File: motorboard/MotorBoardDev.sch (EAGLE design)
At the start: 65 parts, among them J1 Under Glow, J2 B2PS-VH(LF)(SN), J3 B2PS-VH(LF)(SN), J4 B2PS-VH(LF)(SN), Q1 SSM3J338R, Q2 SSM3J338R, Q3 SSM3J338R, Q4 STT4P3LLH6, U1 TXB0104DR, U2 9DoF IMU, U3 TXB0106PWR, U4 TLV70233DBVR, X1 C-GRID-05-15-91, X2 C-GRID-05-15-91, X3 MINI-USB_SHIELD5P4-32005-400, X4 C-GRID-02-70553, X5 SI-50170, X7 2510-, X8 2510-

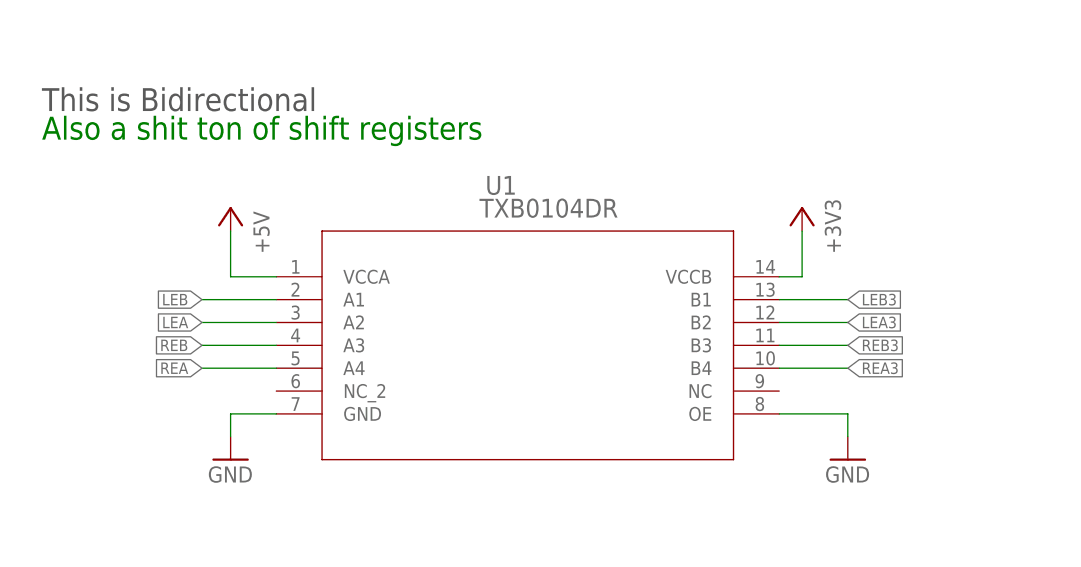
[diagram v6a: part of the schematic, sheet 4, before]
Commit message: Differential and Silkscreen fixed
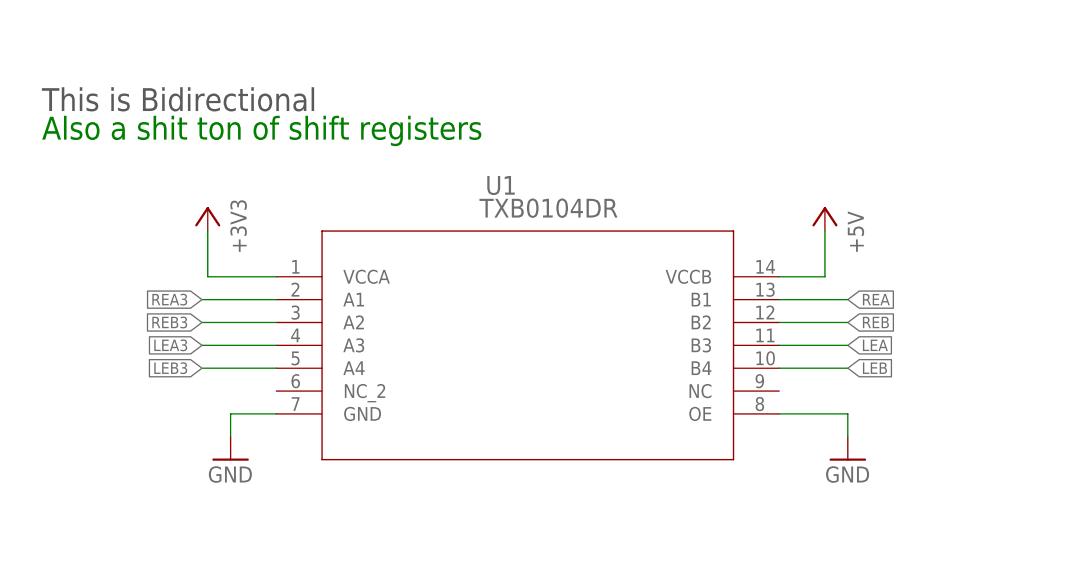
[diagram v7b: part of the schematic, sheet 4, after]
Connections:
- net N$1 renamed SAFETY_HRD
- net N$10 renamed FRONT_HDR
- net N$12 renamed 12V_LED_R
- net N$17 renamed MBED_R_LED1
- net N$18 renamed MBED_R_LED2
- net N$19 renamed GREEN_R
- net N$2 renamed REGOUT_C
- net N$26 renamed RED_R
- net N$29 renamed R_OK3A
- net N$3 renamed INDI_LED_R
- net N$30 renamed R_OK4A
- net N$31 renamed R_OK4B
- net N$32 renamed R_OK3B
- net N$4 renamed BLUE_R
- net N$5 renamed 5V_LED_R
- net N$6 renamed 3V3_LED_R
- net N$7 renamed SAFETY_R
- net N$8 renamed FRONT_R
- net N$9 renamed 24V_LED_R
- net +3V3: now also U1.VCCA; no longer U1.VCCB
- net +5V: now also U1.VCCB; no longer U1.VCCA
- net LEA: now also U1.B3; no longer U1.A2
- net LEA3: now also U1.A3; no longer U1.B2
- net LEB: now also U1.B4; no longer U1.A1
- net LEB3: now also U1.A4; no longer U1.B1
- net REA: now also U1.B1; no longer U1.A4
- net REA3: now also U1.A1; no longer U1.B4
- net REB: now also U1.B2; no longer U1.A3
- net REB3: now also U1.A2; no longer U1.B3
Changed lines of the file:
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@@
 </segment>
 </net>
-<net name="N$17" class="0">
+<net name="MBED_R_LED1" class="0">
 <segment>
 <pinref part="A1" gate="G$1" pin="P$22"/>
@@
 </segment>
 </net>
-<net name="N$18" class="0">
+<net name="MBED_R_LED2" class="0">
 <segment>
 <pinref part="A1" gate="G$1" pin="P$21"/>
@@
 </segment>
 </net>
-<net name="N$3" class="0">
+<net name="INDI_LED_R" class="0">
 <segment>
 <pinref part="D5" gate="G$1" pin="C"/>
@@
 </segment>
 </net>
-<net name="N$2" class="0">
+<net name="REGOUT_C" class="0">
 <segment>
 <pinref part="U2" gate="G$1" pin="REGOUT"/>
@@
 </segment>
 </net>
-<net name="N$29" class="0">
+<net name="R_OK3A" class="0">
 <segment>
 <pinref part="R21" gate="G$1" pin="2"/>
@@
 </segment>
 </net>
-<net name="N$30" class="0">
+<net name="R_OK4A" class="0">
 <segment>
 <pinref part="R22" gate="G$1" pin="2"/>
@@
 </segment>
 </net>
-<net name="N$31" class="0">
+<net name="R_OK4B" class="0">
 <segment>
 <pinref part="R24" gate="G$1" pin="2"/>
@@
 </segment>
 </net>
-<net name="N$32" class="0">
+<net name="R_OK3B" class="0">
 <segment>
 <pinref part="R23" gate="G$1" pin="2"/>
@@
 </segment>
 </net>
-<net name="N$1" class="0">
+<net name="SAFETY_HRD" class="0">
 <segment>
 <wire x1="241.3" y1="91.44" x2="226.06" y2="91.44" width="0.1524" layer="91"/>
@@
 </segment>
 </net>
-<net name="N$5" class="0">
+<net name="5V_LED_R" class="0">
 <segment>
 <pinref part="R5" gate="G$1" pin="1"/>
@@
 </segment>
 </net>
-<net name="N$6" class="0">
+<net name="3V3_LED_R" class="0">
 <segment>
 <pinref part="R7" gate="G$1" pin="1"/>
@@
 </segment>
 </net>
-<net name="N$9" class="0">
+<net name="24V_LED_R" class="0">
 <segment>
 <pinref part="R8" gate="G$1" pin="1"/>
@@
 </segment>
 </net>
-<net name="N$12" class="0">
+<net name="12V_LED_R" class="0">
 <segment>
 <pinref part="R9" gate="G$1" pin="1"/>
@@
 </segment>
 </net>
-<net name="N$19" class="0">
+<net name="GREEN_R" class="0">
 <segment>
 <pinref part="R3" gate="G$1" pin="2"/>
@@
 </segment>
 </net>
-<net name="N$4" class="0">
+<net name="BLUE_R" class="0">
 <segment>
 <pinref part="R2" gate="G$1" pin="2"/>
@@
 </segment>
 </net>
-<net name="N$7" class="0">
+<net name="SAFETY_R" class="0">
 <segment>
 <pinref part="R30" gate="G$1" pin="1"/>
@@
 </segment>
 </net>
-<net name="N$26" class="0">
+<net name="RED_R" class="0">
 <segment>
 <pinref part="R1" gate="G$1" pin="2"/>
@@
 <instance part="GND24" gate="1" x="139.7" y="74.295"/>
 <instance part="U1" gate="A" x="33.02" y="116.84"/>
-<instance part="P+4" gate="1" x="30.48" y="124.46" rot="MR0"/>
-<instance part="+3V4" gate="G$1" x="93.98" y="124.46" rot="MR0"/>
+<instance part="P+4" gate="1" x="96.52" y="124.46" rot="MR0"/>
+<instance part="+3V4" gate="G$1" x="27.94" y="124.46" rot="MR0"/>
 <instance part="GND26" gate="1" x="30.48" y="96.52"/>
 <instance part="GND27" gate="1" x="99.06" y="96.52"/>
@@
 </segment>
 <segment>
-<pinref part="U1" gate="A" pin="VCCB"/>
-<pinref part="+3V4" gate="G$1" pin="+3V3"/>
-<wire x1="91.44" y1="116.84" x2="93.98" y2="116.84" width="0.1524" layer="91"/>
-<wire x1="93.98" y1="116.84" x2="93.98" y2="121.92" width="0.1524" layer="91"/>
-</segment>
-<segment>
 <wire x1="33.02" y1="50.8" x2="20.32" y2="50.8" width="0.1524" layer="91"/>
 <pinref part="+3V5" gate="G$1" pin="+3V3"/>
@@
 <pinref part="U3" gate="A" pin="VCCA"/>
 </segment>
+<segment>
+<pinref part="+3V4" gate="G$1" pin="+3V3"/>
+<wire x1="27.94" y1="121.92" x2="27.94" y2="116.84" width="0.1524" layer="91"/>
+<pinref part="U1" gate="A" pin="VCCA"/>
+<wire x1="27.94" y1="116.84" x2="35.56" y2="116.84" width="0.1524" layer="91"/>
+</segment>
 </net>
 <net name="RD-" class="0">
@@
 </segment>
 </net>
-<net name="LEB" class="0">
-<segment>
-<pinref part="U1" gate="A" pin="A1"/>
-<wire x1="35.56" y1="114.3" x2="27.305" y2="114.3" width="0.1524" layer="91"/>
-<label x="27.305" y="114.3" size="1.27" layer="95" rot="R180" xref="yes"/>
-</segment>
-</net>
 <net name="REB" class="0">
 <segment>
-<pinref part="U1" gate="A" pin="A3"/>
-<wire x1="35.56" y1="109.22" x2="27.305" y2="109.22" width="0.1524" layer="91"/>
-<label x="27.305" y="109.22" size="1.27" layer="95" rot="R180" xref="yes"/>
+<pinref part="U1" gate="A" pin="B2"/>
+<wire x1="91.44" y1="111.76" x2="99.06" y2="111.76" width="0.1524" layer="91"/>
+<label x="99.06" y="111.76" size="1.27" layer="95" xref="yes"/>
 </segment>
 </net>
@@
 <wire x1="251.46" y1="187.96" x2="256.54" y2="187.96" width="0.1524" layer="91"/>
 <junction x="256.54" y="187.96"/>
-</segment>
-<segment>
-<pinref part="P+4" gate="1" pin="+5V"/>
-<pinref part="U1" gate="A" pin="VCCA"/>
-<wire x1="30.48" y1="121.92" x2="30.48" y2="116.84" width="0.1524" layer="91"/>
-<wire x1="30.48" y1="116.84" x2="35.56" y2="116.84" width="0.1524" layer="91"/>
 </segment>
 <segment>
@@
 <junction x="220.98" y="137.16"/>
 </segment>
+<segment>
+<pinref part="U1" gate="A" pin="VCCB"/>
+<pinref part="P+4" gate="1" pin="+5V"/>
+<wire x1="96.52" y1="121.92" x2="96.52" y2="116.84" width="0.1524" layer="91"/>
+<wire x1="96.52" y1="116.84" x2="91.44" y2="116.84" width="0.1524" layer="91"/>
+</segment>
 </net>
 <net name="LEB3" class="0">
 <segment>
-<pinref part="U1" gate="A" pin="B1"/>
-<wire x1="91.44" y1="114.3" x2="99.06" y2="114.3" width="0.1524" layer="91"/>
-<label x="99.06" y="114.3" size="1.27" layer="95" xref="yes"/>
-</segment>
-</net>
-<net name="REB3" class="0">
-<segment>
-<pinref part="U1" gate="A" pin="B3"/>
-<wire x1="91.44" y1="109.22" x2="99.06" y2="109.22" width="0.1524" layer="91"/>
-<label x="99.06" y="109.22" size="1.27" layer="95" xref="yes"/>
+<pinref part="U1" gate="A" pin="A4"/>
+<wire x1="35.56" y1="106.68" x2="27.305" y2="106.68" width="0.1524" layer="91"/>
+<label x="27.305" y="106.68" size="1.27" layer="95" rot="R180" xref="yes"/>
 </segment>
 </net>
@@
 </segment>
 </net>
-<net name="N$10" class="0">
+<net name="FRONT_HDR" class="0">
 <segment>
 <pinref part="X4" gate="-1" pin="S"/>
@@
 </segment>
 </net>
-<net name="N$8" class="0">
+<net name="FRONT_R" class="0">
 <segment>
 <pinref part="R4" gate="G$1" pin="2"/>
@@
 <net name="REA" class="0">
 <segment>
-<pinref part="U1" gate="A" pin="A4"/>
-<wire x1="35.56" y1="106.68" x2="27.305" y2="106.68" width="0.1524" layer="91"/>
-<label x="27.305" y="106.68" size="1.27" layer="95" rot="R180" xref="yes"/>
+<pinref part="U1" gate="A" pin="B1"/>
+<wire x1="91.44" y1="114.3" x2="99.06" y2="114.3" width="0.1524" layer="91"/>
+<label x="99.06" y="114.3" size="1.27" layer="95" xref="yes"/>
+</segment>
+</net>
+<net name="REB3" class="0">
+<segment>
+<pinref part="U1" gate="A" pin="A2"/>
+<wire x1="35.56" y1="111.76" x2="27.305" y2="111.76" width="0.1524" layer="91"/>
+<label x="27.305" y="111.76" size="1.27" layer="95" rot="R180" xref="yes"/>
 </segment>
 </net>
 <net name="REA3" class="0">
+<segment>
+<pinref part="U1" gate="A" pin="A1"/>
+<wire x1="35.56" y1="114.3" x2="27.305" y2="114.3" width="0.1524" layer="91"/>
+<label x="27.305" y="114.3" size="1.27" layer="95" rot="R180" xref="yes"/>
+</segment>
+</net>
+<net name="LEA3" class="0">
+<segment>
+<pinref part="U1" gate="A" pin="A3"/>
+<wire x1="35.56" y1="109.22" x2="27.305" y2="109.22" width="0.1524" layer="91"/>
+<label x="27.305" y="109.22" size="1.27" layer="95" rot="R180" xref="yes"/>
+</segment>
+</net>
+<net name="LEA" class="0">
+<segment>
+<pinref part="U1" gate="A" pin="B3"/>
+<wire x1="91.44" y1="109.22" x2="99.06" y2="109.22" width="0.1524" layer="91"/>
+<label x="99.06" y="109.22" size="1.27" layer="95" xref="yes"/>
+</segment>
+</net>
+<net name="LEB" class="0">
 <segment>
 <pinref part="U1" gate="A" pin="B4"/>
@@
 </segment>
 </net>
-<net name="LEA3" class="0">
-<segment>
-<pinref part="U1" gate="A" pin="B2"/>
-<wire x1="91.44" y1="111.76" x2="99.06" y2="111.76" width="0.1524" layer="91"/>
-<label x="99.06" y="111.76" size="1.27" layer="95" xref="yes"/>
-</segment>
-</net>
-<net name="LEA" class="0">
-<segment>
-<pinref part="U1" gate="A" pin="A2"/>
-<wire x1="35.56" y1="111.76" x2="27.305" y2="111.76" width="0.1524" layer="91"/>
-<label x="27.305" y="111.76" size="1.27" layer="95" rot="R180" xref="yes"/>
-</segment>
-</net>

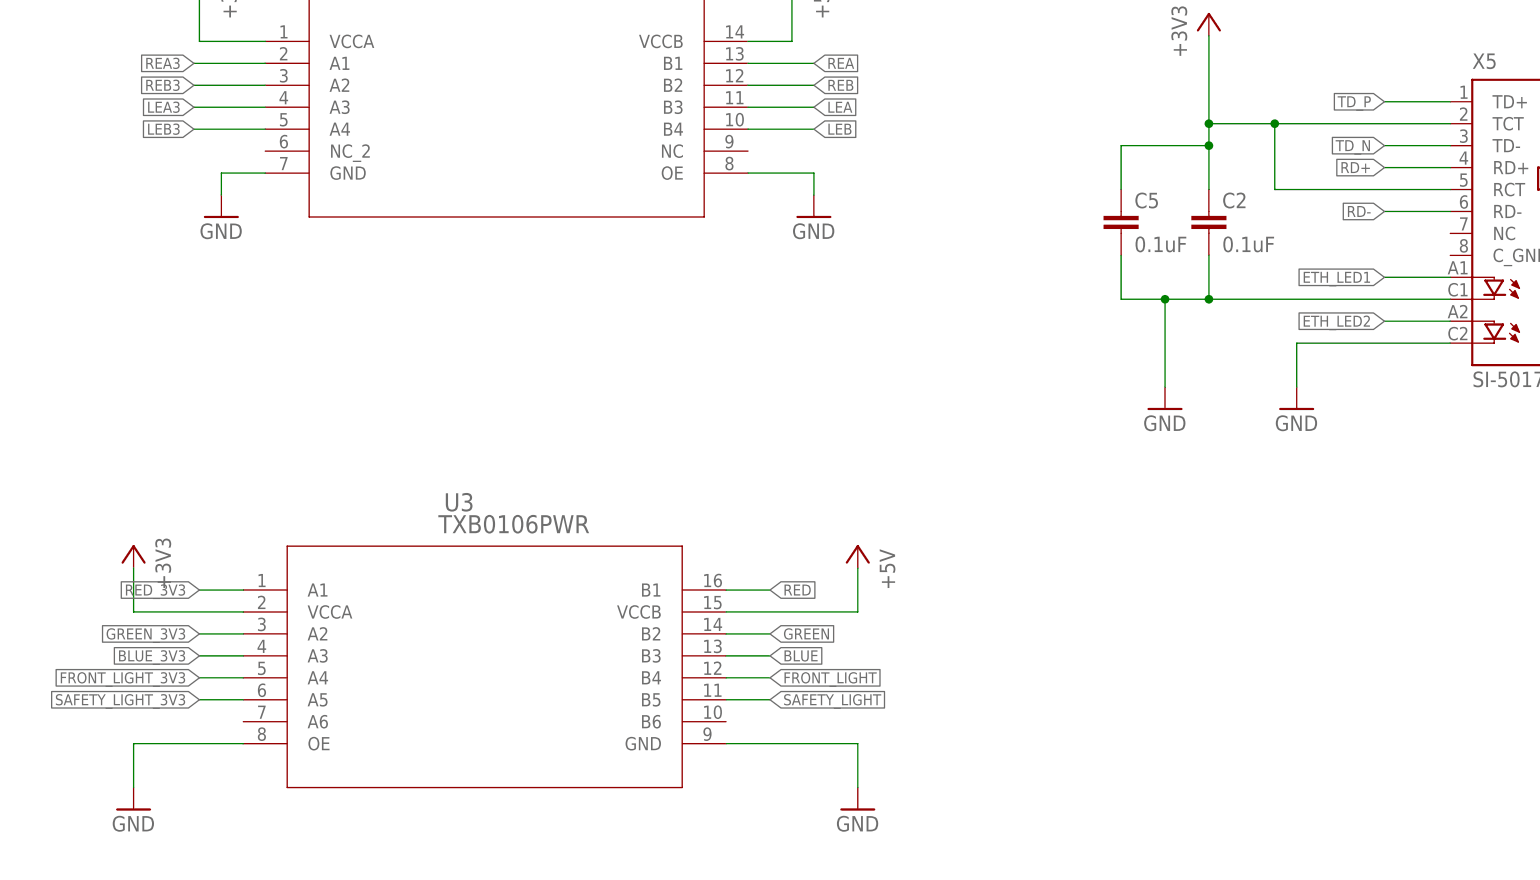
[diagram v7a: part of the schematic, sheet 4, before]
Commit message: changed front light to flood light
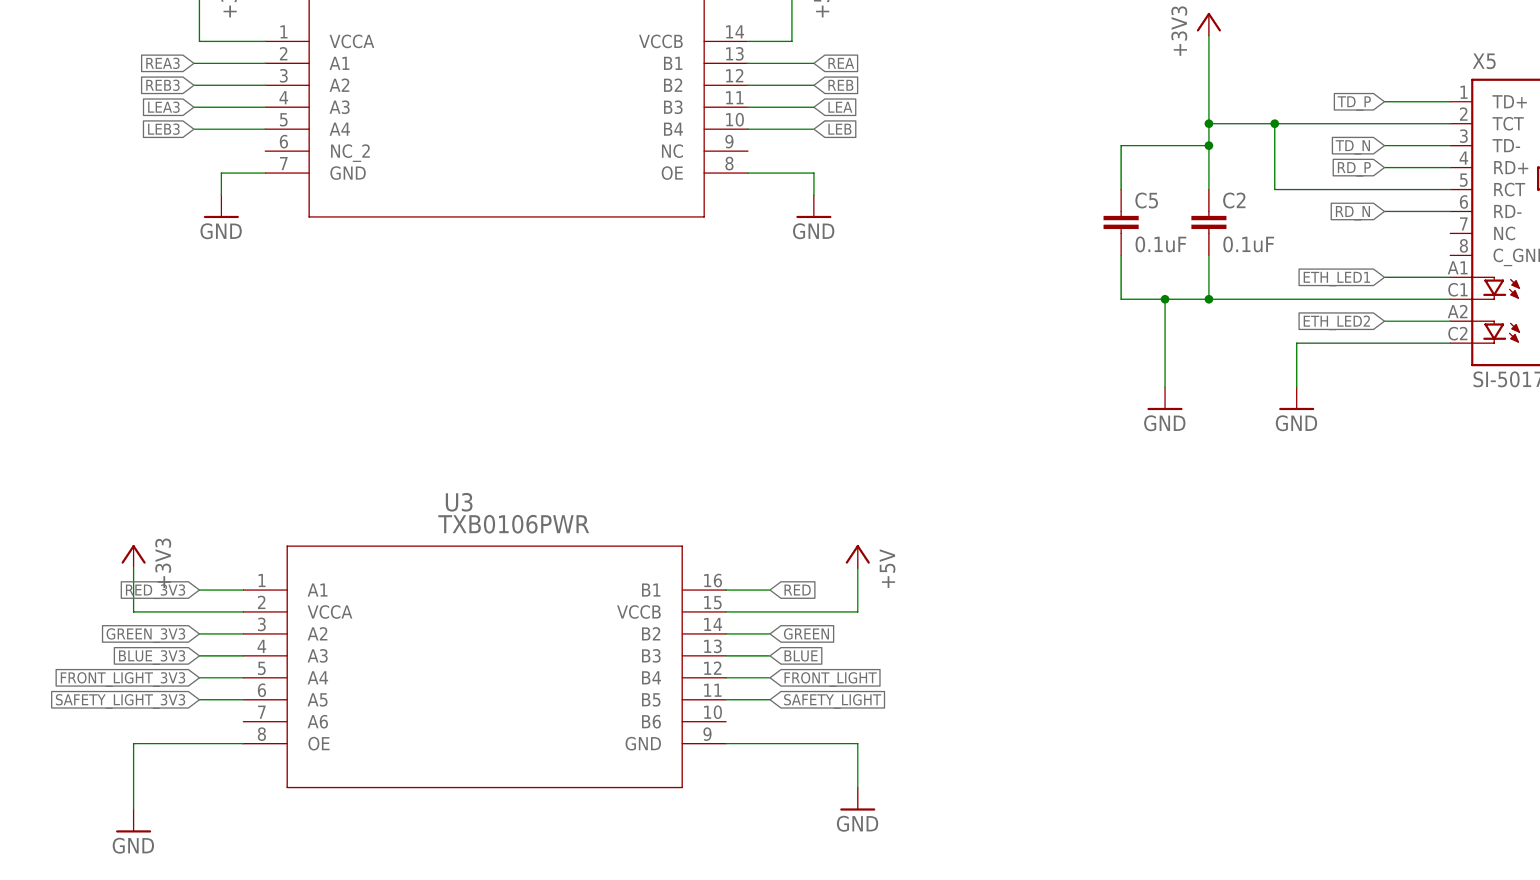
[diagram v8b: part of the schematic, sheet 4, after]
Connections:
- net RD+ renamed RD_P
- net RD- renamed RD_N
- net GND: now also U3.GND, U3.OE
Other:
- note added: "Flood Light"
- note removed: "E-Stop Status"
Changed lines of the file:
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@@
 <layer number="94" name="Symbols" color="4" fill="1" visible="yes" active="yes"/>
 <layer number="95" name="Names" color="7" fill="1" visible="yes" active="yes"/>
-<layer number="96" name="Values" color="7" fill="1" visible="no" active="yes"/>
+<layer number="96" name="Values" color="7" fill="1" visible="yes" active="yes"/>
 <layer number="97" name="Info" color="7" fill="1" visible="yes" active="yes"/>
 <layer number="98" name="Guide" color="6" fill="1" visible="yes" active="yes"/>
@@
 </segment>
 </net>
-<net name="RD-" class="0">
+<net name="RD_N" class="0">
 <segment>
 <wire x1="177.8" y1="127" x2="193.04" y2="127" width="0.1524" layer="91"/>
@@
 </segment>
 </net>
-<net name="RD+" class="0">
+<net name="RD_P" class="0">
 <segment>
 <wire x1="177.8" y1="124.46" x2="193.04" y2="124.46" width="0.1524" layer="91"/>
@@
 <instance part="GND8" gate="1" x="208.28" y="157.48"/>
 <instance part="GND11" gate="1" x="208.28" y="172.72"/>
-<instance part="Q1" gate="G$1" x="50.8" y="149.86"/>
-<instance part="Q2" gate="G$1" x="99.06" y="149.86"/>
-<instance part="Q3" gate="G$1" x="144.78" y="149.86"/>
+<instance part="Q1" gate="G$1" x="50.8" y="149.86" smashed="yes">
+<attribute name="VALUE" x="35.56" y="144.78" size="1.778" layer="96"/>
+<attribute name="NAME" x="53.34" y="152.4" size="1.778" layer="95"/>
+</instance>
+<instance part="Q2" gate="G$1" x="99.06" y="149.86" smashed="yes">
+<attribute name="VALUE" x="83.82" y="144.78" size="1.778" layer="96"/>
+<attribute name="NAME" x="101.6" y="152.4" size="1.778" layer="95"/>
+</instance>
+<instance part="Q3" gate="G$1" x="144.78" y="149.86" smashed="yes">
+<attribute name="VALUE" x="129.54" y="144.78" size="1.778" layer="96"/>
+<attribute name="NAME" x="147.32" y="152.4" size="1.778" layer="95"/>
+</instance>
 <instance part="J2" gate="G$1" x="246.38" y="88.9" rot="R180"/>
 <instance part="Q4" gate="A" x="226.06" y="99.06"/>
@@
 <wire x1="118.11" y1="5.08" x2="7.62" y2="5.08" width="0.1524" layer="103" style="shortdash"/>
 <wire x1="7.62" y1="5.08" x2="7.62" y2="139.7" width="0.1524" layer="103" style="shortdash"/>
-<text x="168.91" y="146.05" size="2.54" layer="103" font="vector">E-Stop Status</text>
+<text x="176.53" y="146.05" size="2.54" layer="103" font="vector">Flood Light</text>
 <text x="168.91" y="50.8" size="2.54" layer="103" font="vector">Ethernet Header</text>
 <wire x1="104.14" y1="208.28" x2="203.2" y2="208.28" width="0.1524" layer="103" style="shortdash"/>
@@
 <instance part="J3" gate="G$1" x="43.18" y="179.07" rot="R180"/>
 <instance part="J4" gate="G$1" x="70.485" y="179.07" rot="R180"/>
-<instance part="GND7" gate="1" x="20.32" y="27.94"/>
+<instance part="GND7" gate="1" x="20.32" y="25.4"/>
 <instance part="U3" gate="A" x="30.48" y="53.34"/>
 <instance part="U$8" gate="A" x="154.94" y="182.88"/>
@@
 <segment>
 <pinref part="GND7" gate="1" pin="GND"/>
-<wire x1="20.32" y1="30.48" x2="20.32" y2="35.56" width="0.1524" layer="91"/>
-<wire x1="20.32" y1="35.56" x2="33.02" y2="35.56" width="0.1524" layer="91"/>
+<wire x1="20.32" y1="27.94" x2="20.32" y2="35.56" width="0.1524" layer="91"/>
+<pinref part="U3" gate="A" pin="OE"/>
+<wire x1="33.02" y1="35.56" x2="20.32" y2="35.56" width="0.1524" layer="91"/>
 </segment>
 <segment>
@@
 <wire x1="104.14" y1="30.48" x2="104.14" y2="35.56" width="0.1524" layer="91"/>
 <wire x1="104.14" y1="35.56" x2="88.9" y2="35.56" width="0.1524" layer="91"/>
+<pinref part="U3" gate="A" pin="GND"/>
 </segment>
 </net>
@@
 </segment>
 </net>
-<net name="RD-" class="0">
+<net name="RD_N" class="0">
 <segment>
 <pinref part="X5" gate="G$1" pin="RD-"/>
@@
 </segment>
 </net>
-<net name="RD+" class="0">
+<net name="RD_P" class="0">
 <segment>
 <pinref part="X5" gate="G$1" pin="RD+"/>
